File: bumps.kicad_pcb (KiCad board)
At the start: 2 copper layers, 111.1 x 65.4 mm, 137 parts, among them M1 CONN_1, M2 CONN_1, M3 CONN_1, P1 DIL6, P10 Mot-A, P11 Mot-A, P12 Mot-X, P13 T1, P14 T2, P15 T3, P16 MPower, P17 PWM-2, P18 PWM-1, P19 END-X, P2 DIL6, P20 END-Y, P21 END-Z, P22 Mot-X, P23 Mot-Y, P24 Mot-Y, P25 Mot-Z, P26 Mot-Z, P27 Aux, P29 PWM, P3 Mot-E, P4 Mot-E, P5 DIL6, P6 DIL6, P7 DIL6, P8 P8 Header, P9 P9 Header, Q1 IRLB8743PBF, Q2 IRLB8743PBF, Q3 FDS9926A, Q4 FDS9926A, U1 E-Polo, U2 A-Polo, U3 X-Polo, U4 Y-Polo, U5 Z-Polo, U6 MC34063, U7 AP1117/3.3

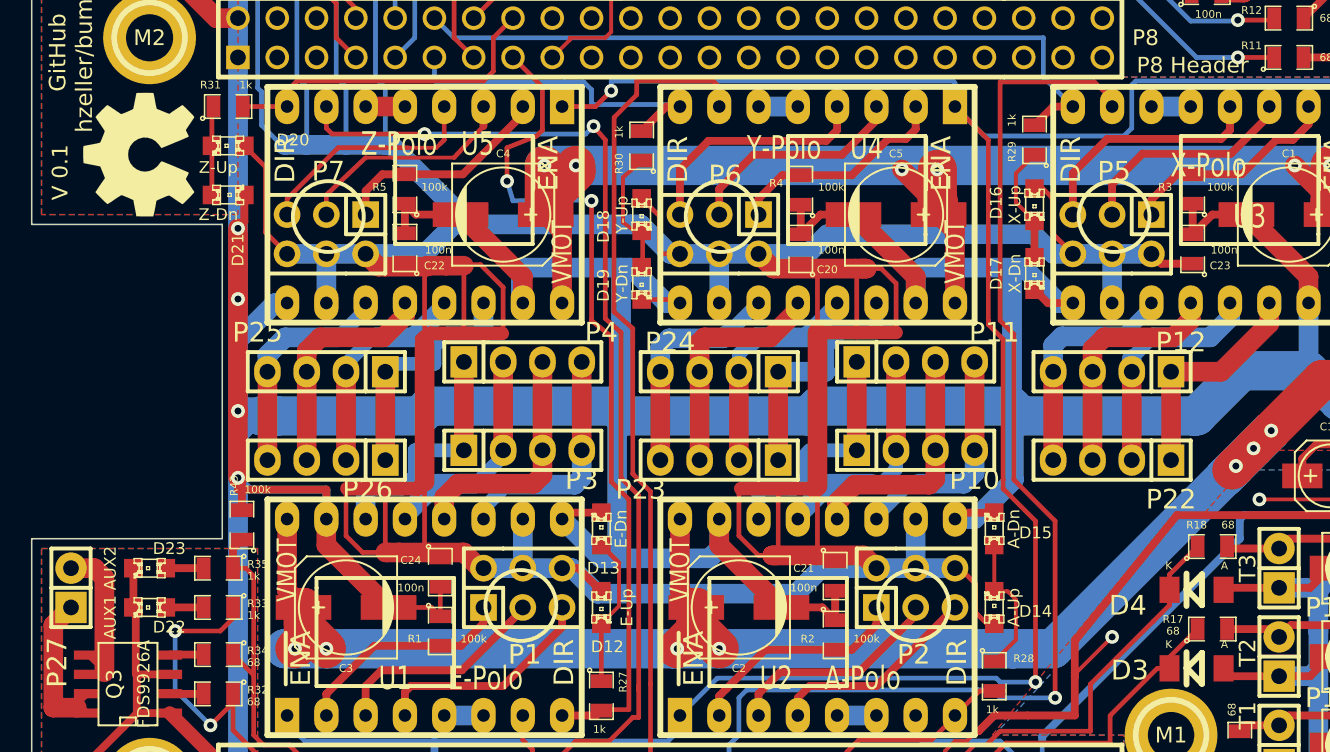
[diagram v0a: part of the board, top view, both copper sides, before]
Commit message: o Get rid of 100k pull-down for MS1. Not needed   (fixes #9)
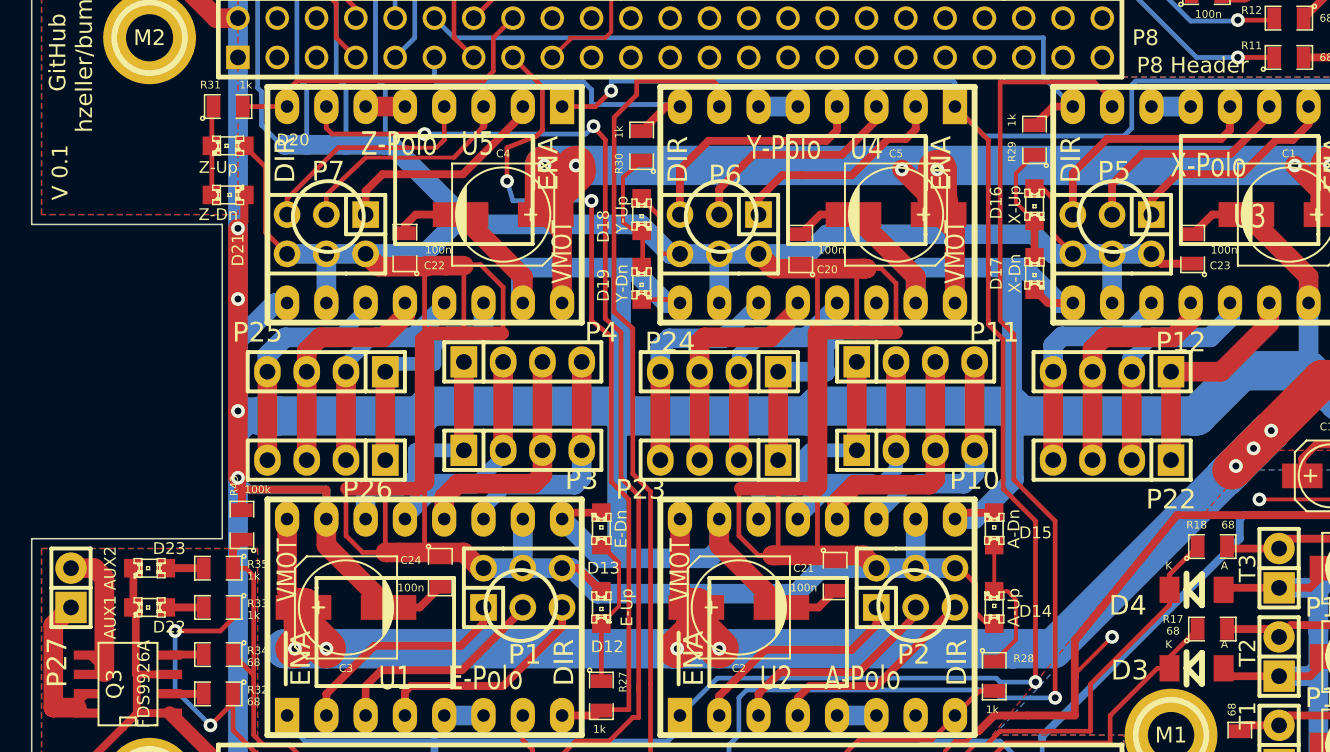
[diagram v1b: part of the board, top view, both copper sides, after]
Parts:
- removed G***: LOGO, bumps:OSH-LOGO
- removed R1, R2, R3, R4, R5: 100k, SMD_Packages:SM0805
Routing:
- net GND: track 835.4 -> 826.8 mm

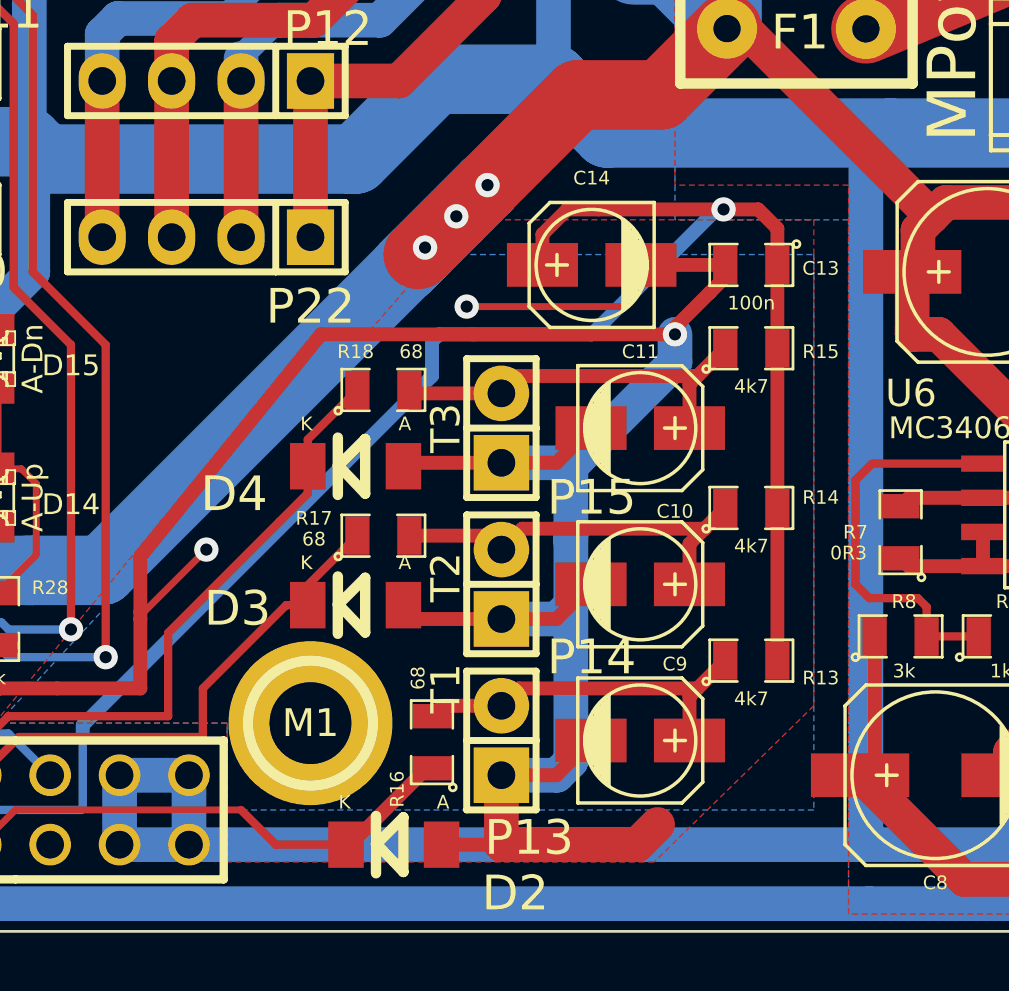
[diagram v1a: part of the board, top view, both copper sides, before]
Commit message: o Use 10uF ceramic capacitors in analog section. Makes that part more   compact and nicer to assemble.   Fixes #7
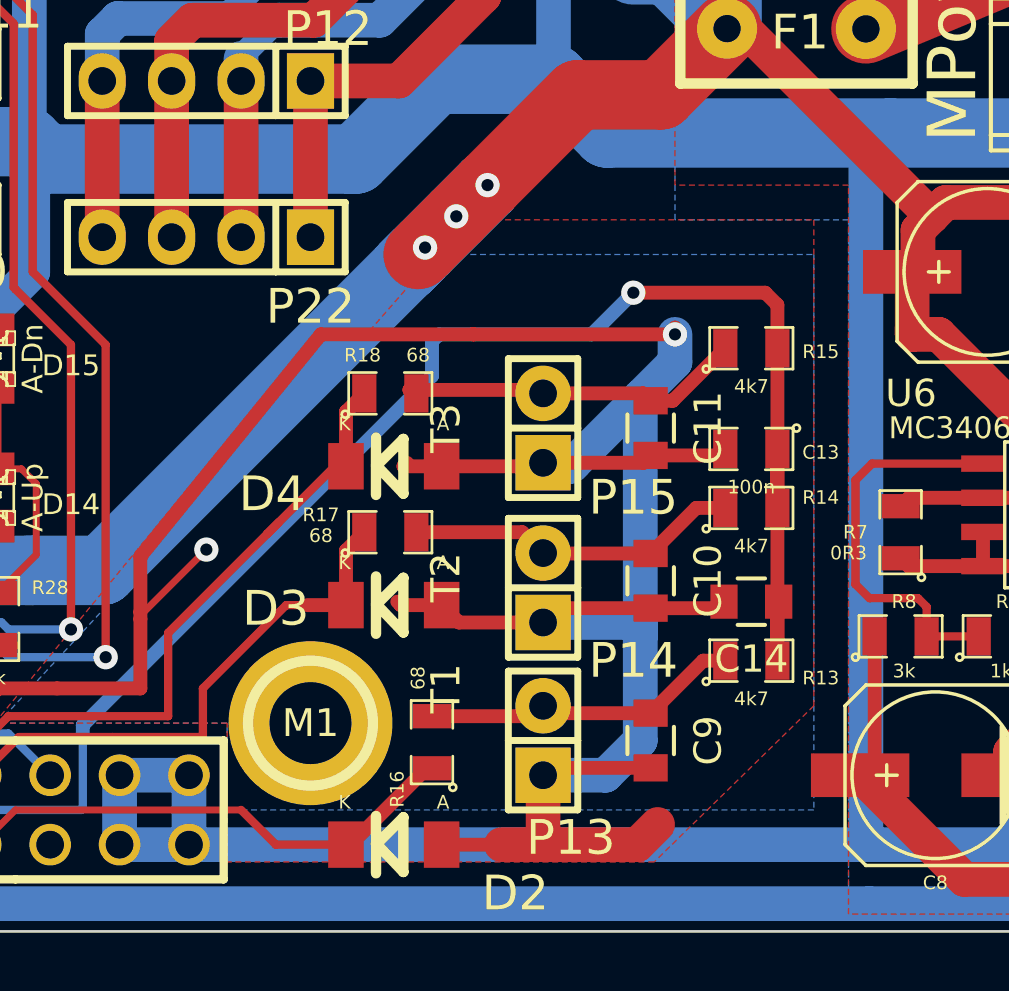
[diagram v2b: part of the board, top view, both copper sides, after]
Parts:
- C10, C11, C14, C9: footprint Capacitors_SMD:c_elec_4x5.7 -> Capacitors_SMD:C_0805
- moved C14 13.6 mm to (137.4, 81.3)
- moved C13 6.73 mm to (137.4, 75.7)
- moved P14 1.53 mm to (129.8, 80.8)
- moved P13 1.52 mm to (129.8, 86.4)
- moved P15 1.52 mm to (129.8, 74.9)
- moved D3 1.40 mm to (124.3, 81.4)
- moved D4 1.40 mm to (124.3, 76.3)
- moved C10 0.40 mm to (133.7, 80.5), turned to 270 degrees
- moved C11 0.38 mm to (133.7, 74.9), turned to 270 degrees
- moved C9 0.38 mm to (133.7, 86.4), turned to 270 degrees
- moved R17 0.28 mm to (124.2, 78.7)
- moved R18 0.28 mm to (124.2, 73.7)
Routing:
- net VDD_ADC: track 75.8 -> 67.9 mm
- net Net-(C10-Pad1): track 14.7 -> 12.5 mm
- net Net-(C11-Pad1): track 14.3 -> 12.8 mm
- net Net-(C9-Pad1): track 13.6 -> 12.3 mm
- net TEMP_2: track 18.9 -> 20.0 mm
- net TEMP_3: track 27.3 -> 28.1 mm
- net AGND: track 124.0 -> 124.4 mm, vias 3 -> 2
